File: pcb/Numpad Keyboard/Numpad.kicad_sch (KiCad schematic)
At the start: 57 parts

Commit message: Updated library
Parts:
- U?: symbol Interface_Expansion:MCP23S17_SO -> vakeyboard:MCP23S17_SO; Description / Value (none) -> 10MHz 16 POR SPI SOIC-28_300mil I/O Expanders ROHS; LCSC (none) -> C47023; Manufacturer (none) -> Microchip Tech; Mfg Part # (none) -> MCP23S17T-E/SO; Package/Footprint (none) -> SOIC-28_7.5x17.9x1.27P; Type (none) -> SMD
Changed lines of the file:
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@@
     (pin "2")
   )
-  (symbol (lib_id "Interface_Expansion:MCP23S17_SO") (at 151.13 73.66 0) (unit 1)
+  (symbol (lib_id "vakeyboard:MCP23S17_SO") (at 151.13 73.66 0) (unit 1)
     (in_bom yes) (on_board yes) (fields_autoplaced)
     (property "Reference" "U?" (id 0) (at 153.1494 45.72 0)
@@
       (effects (font (size 1.27 1.27)) (justify left) hide)
     )
+    (property "Description / Value" "10MHz 16 POR SPI SOIC-28_300mil  I/O Expanders ROHS" (id 4) (at 151.13 73.66 0)
+      (effects (font (size 1.27 1.27)) hide)
+    )
+    (property "LCSC" "C47023" (id 5) (at 151.13 73.66 0)
+      (effects (font (size 1.27 1.27)) hide)
+    )
+    (property "Manufacturer" "Microchip Tech" (id 6) (at 151.13 73.66 0)
+      (effects (font (size 1.27 1.27)) hide)
+    )
+    (property "Mfg Part #" "MCP23S17T-E/SO" (id 7) (at 151.13 73.66 0)
+      (effects (font (size 1.27 1.27)) hide)
+    )
+    (property "Package/Footprint" "SOIC-28_7.5x17.9x1.27P" (id 8) (at 151.13 73.66 0)
+      (effects (font (size 1.27 1.27)) hide)
+    )
+    (property "Type" "SMD" (id 9) (at 151.13 73.66 0)
+      (effects (font (size 1.27 1.27)) hide)
+    )
+    (property "Your Instructions / Notes" "" (id 10) (at 151.13 73.66 0)
+      (effects (font (size 1.27 1.27)) hide)
+    )
     (pin "1")

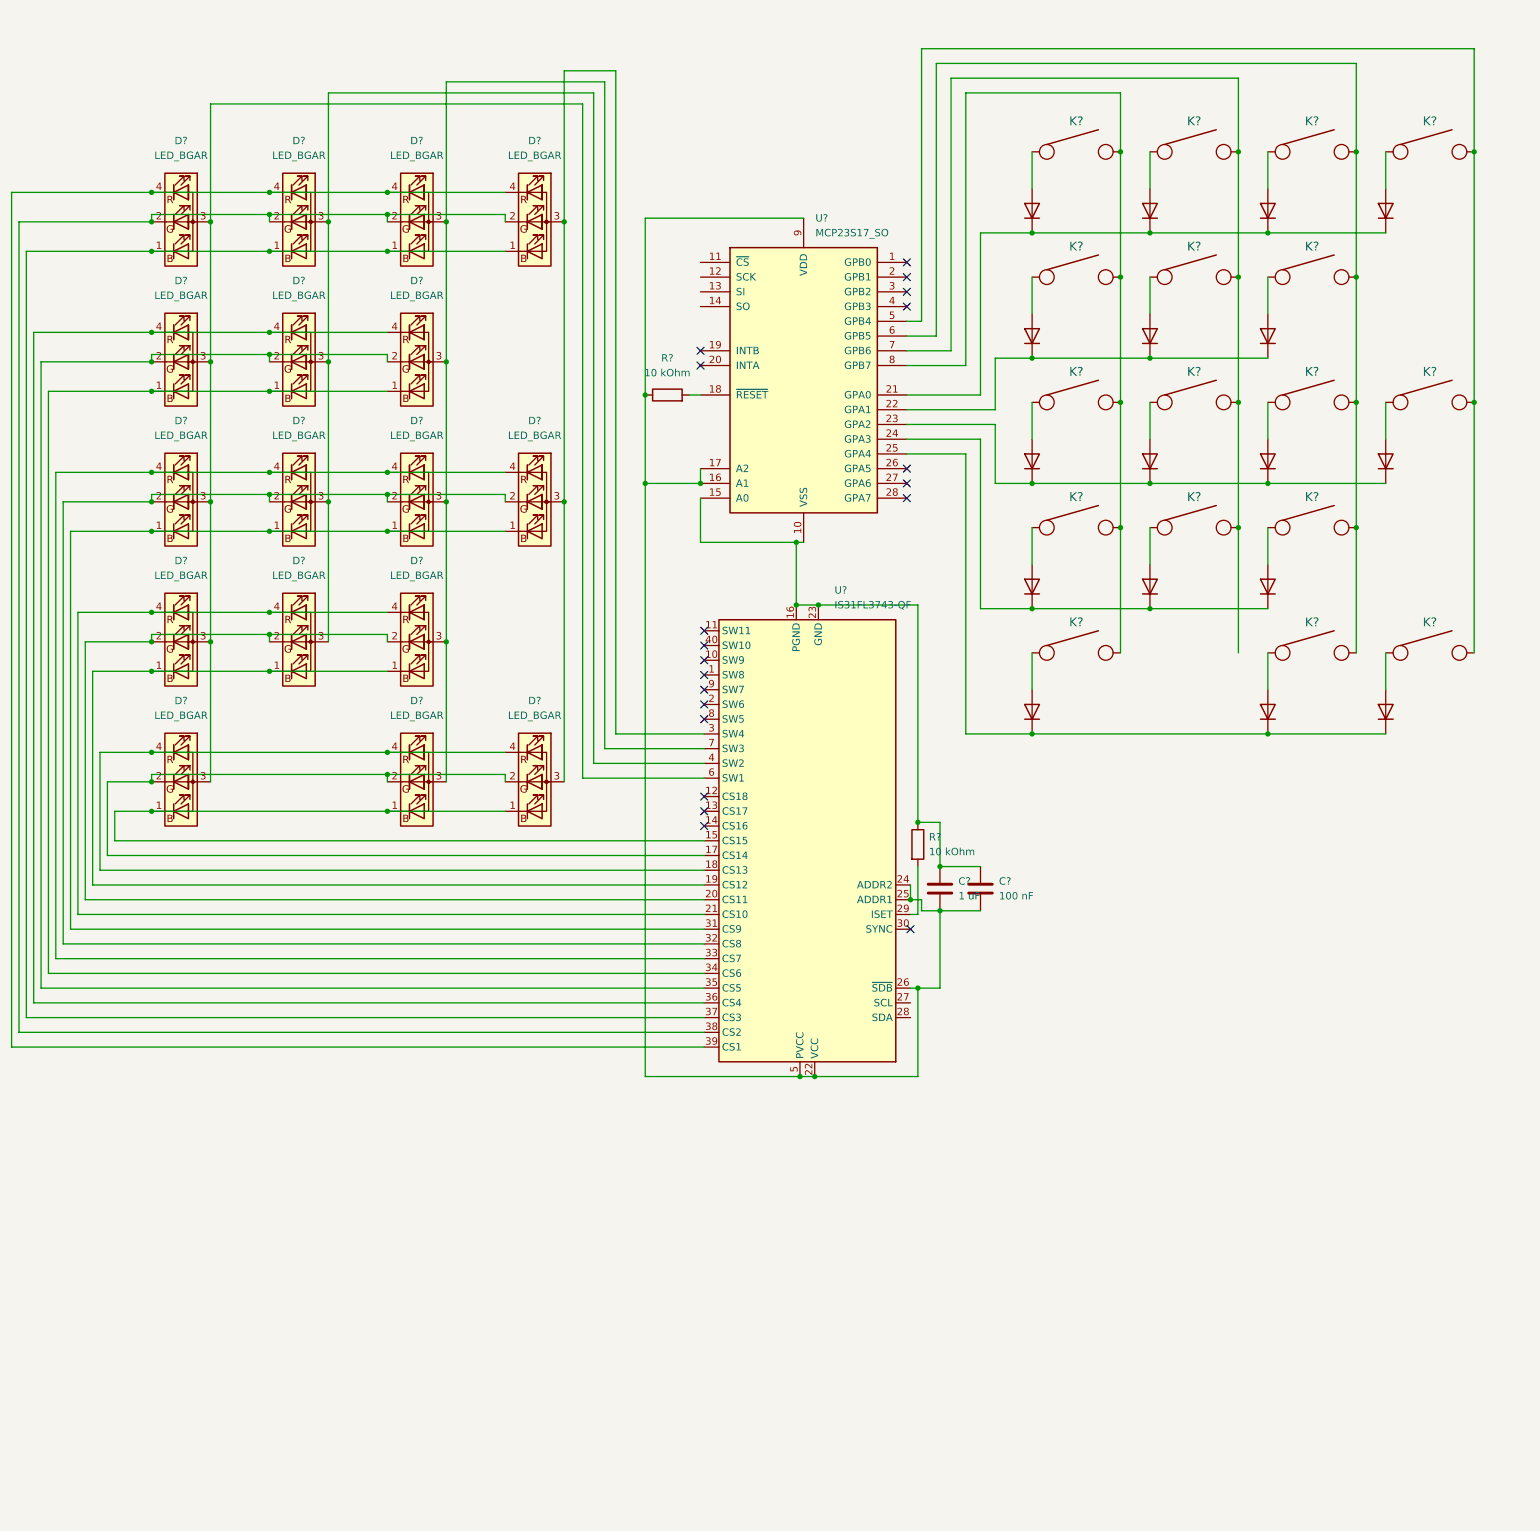
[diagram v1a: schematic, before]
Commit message: Mostly finished tracks for numpad
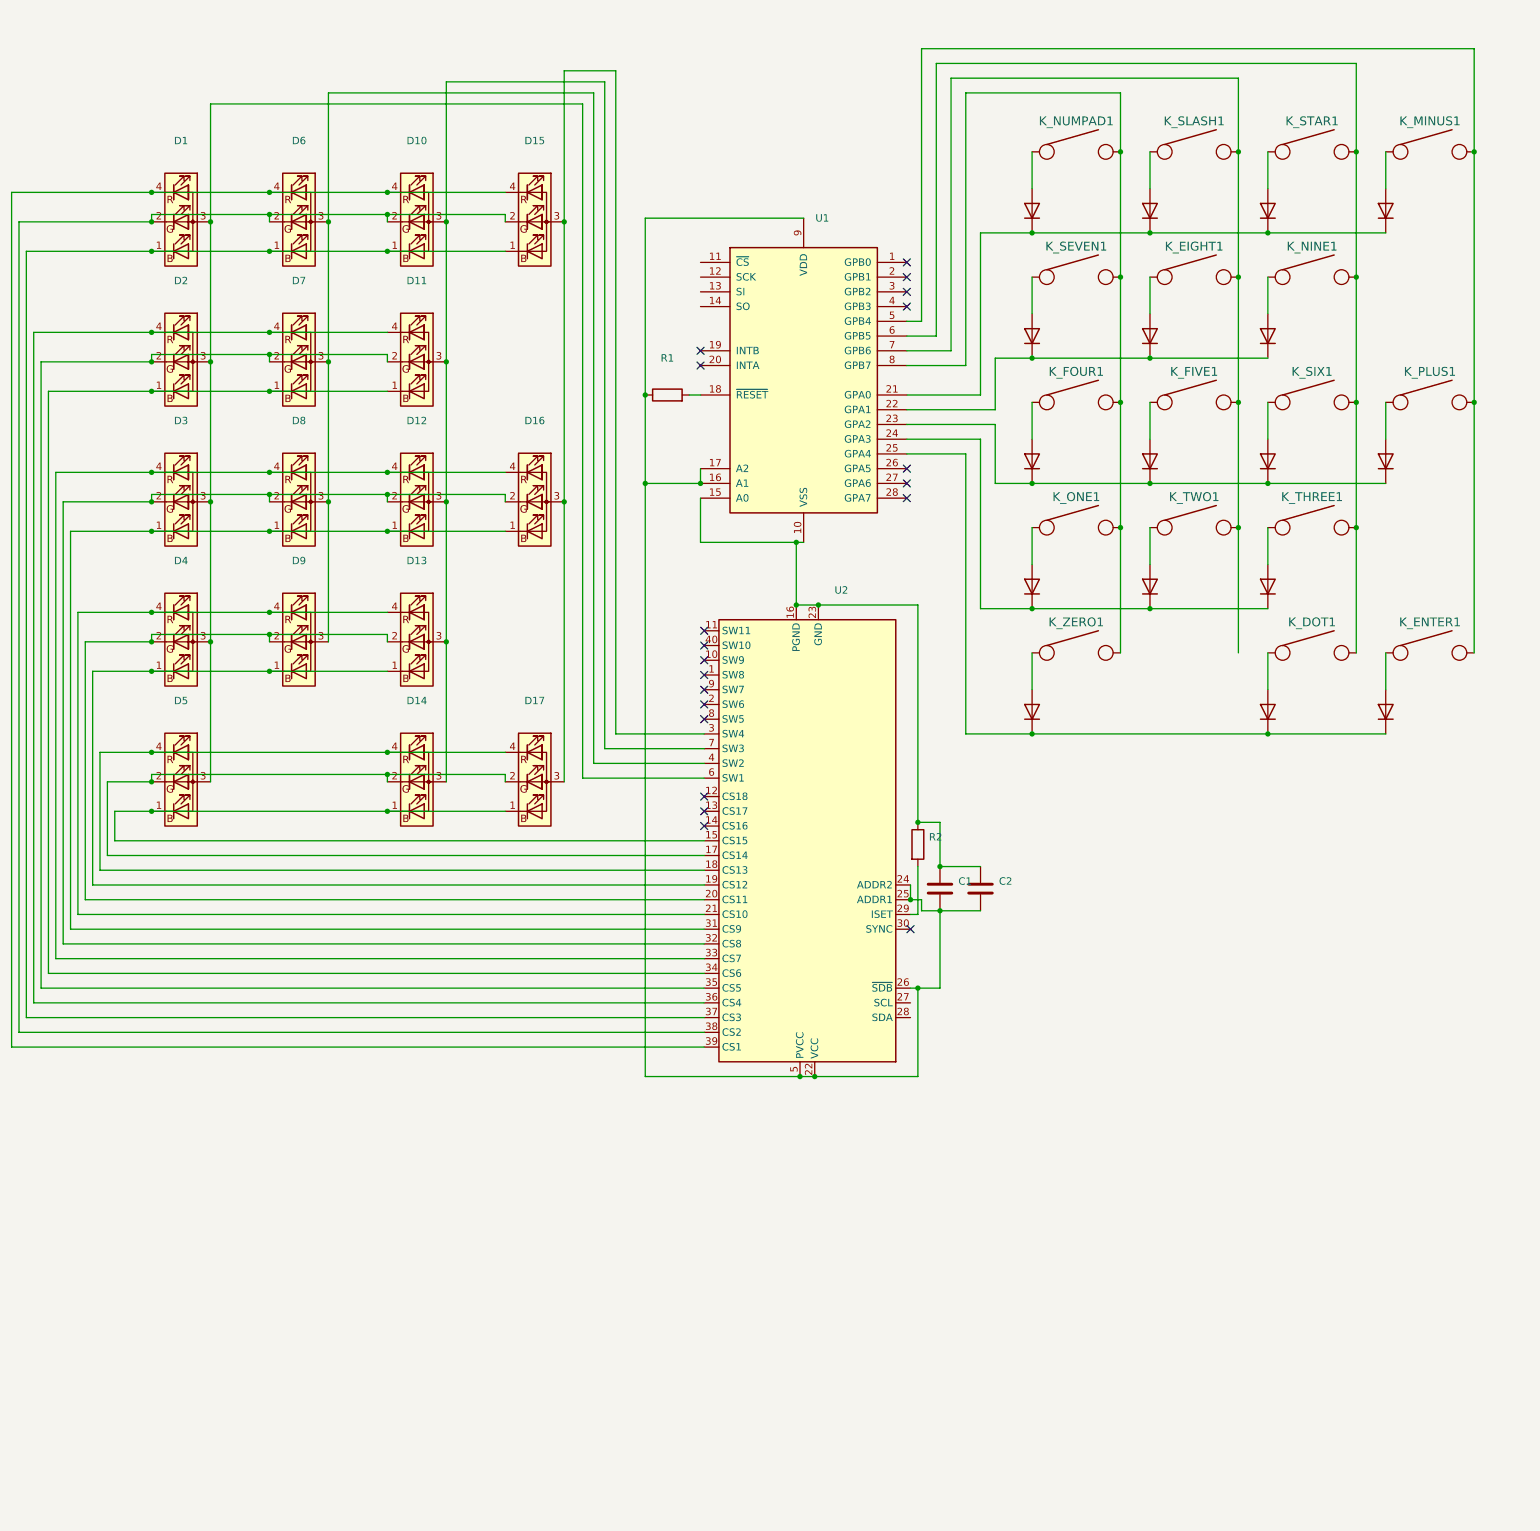
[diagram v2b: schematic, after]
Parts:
- C1: renamed from C?; value 1 uF -> C 1uF; footprint (none) -> Footprints:C_0402_1005Metric; symbol Device:C -> vakeyboard:C 1uF; Description / Value (none) -> 25V 1uF X5R ±10% 0402 Multilayer Ceramic Capacitors MLCC - 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; LCSC (none) -> C52923; Manufacturer (none) -> Samsung Electro-Mechanics; Mfg Part # (none) -> CL05A105KA5NQNC; Package/Footprint (none) -> 0402; Type (none) -> SMD
- C2: renamed from C?; value 100 nF -> C_100nF; footprint (none) -> Footprints:C_0402_1005Metric; symbol Device:C -> vakeyboard:C_100nF; Description / Value (none) -> 16V 100nF X7R ±10% 0402 Multilayer Ceramic Capacitors MLCC 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; LCSC (none) -> C1525; Manufacturer (none) -> Samsung Electro-Mechanics; Mfg Part # (none) -> CL05B104KO5NNNC; Package/Footprint (none) -> 0402; Type (none) -> SMD
- D1: renamed from D?; value LED_BGAR -> LED_NUMPAD; footprint (none) -> Footprints:19-237; symbol Device:LED_BGAR -> vakeyboard:LED; Description / Value (none) -> 5mA Colorless transparence -40℃~+85℃ Common anode RGB 120° 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; LCSC (none) -> C883183; Manufacturer (none) -> Everlight Elec; Mfg Part # (none) -> 19-237/R6GHBHC-A04/2T; Package/Footprint (none) -> 19-237; Type (none) -> SMD
- D10: renamed from D?; value LED_BGAR -> LED_STAR; footprint (none) -> Footprints:19-237; symbol Device:LED_BGAR -> vakeyboard:LED; Description / Value (none) -> 5mA Colorless transparence -40℃~+85℃ Common anode RGB 120° 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; LCSC (none) -> C883183; Manufacturer (none) -> Everlight Elec; Mfg Part # (none) -> 19-237/R6GHBHC-A04/2T; Package/Footprint (none) -> 19-237; Type (none) -> SMD
- D11: renamed from D?; value LED_BGAR -> LED9; footprint (none) -> Footprints:19-237; symbol Device:LED_BGAR -> vakeyboard:LED; Description / Value (none) -> 5mA Colorless transparence -40℃~+85℃ Common anode RGB 120° 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; LCSC (none) -> C883183; Manufacturer (none) -> Everlight Elec; Mfg Part # (none) -> 19-237/R6GHBHC-A04/2T; Package/Footprint (none) -> 19-237; Type (none) -> SMD
- D12: renamed from D?; value LED_BGAR -> LED_6; footprint (none) -> Footprints:19-237; symbol Device:LED_BGAR -> vakeyboard:LED; Description / Value (none) -> 5mA Colorless transparence -40℃~+85℃ Common anode RGB 120° 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; LCSC (none) -> C883183; Manufacturer (none) -> Everlight Elec; Mfg Part # (none) -> 19-237/R6GHBHC-A04/2T; Package/Footprint (none) -> 19-237; Type (none) -> SMD
- D13: renamed from D?; value LED_BGAR -> LED_3; footprint (none) -> Footprints:19-237; symbol Device:LED_BGAR -> vakeyboard:LED; Description / Value (none) -> 5mA Colorless transparence -40℃~+85℃ Common anode RGB 120° 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; LCSC (none) -> C883183; Manufacturer (none) -> Everlight Elec; Mfg Part # (none) -> 19-237/R6GHBHC-A04/2T; Package/Footprint (none) -> 19-237; Type (none) -> SMD
- D14: renamed from D?; value LED_BGAR -> LED_DOT; footprint (none) -> Footprints:19-237; symbol Device:LED_BGAR -> vakeyboard:LED; Description / Value (none) -> 5mA Colorless transparence -40℃~+85℃ Common anode RGB 120° 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; LCSC (none) -> C883183; Manufacturer (none) -> Everlight Elec; Mfg Part # (none) -> 19-237/R6GHBHC-A04/2T; Package/Footprint (none) -> 19-237; Type (none) -> SMD
- D15: renamed from D?; value LED_BGAR -> LED_MINUS; footprint (none) -> Footprints:19-237; symbol Device:LED_BGAR -> vakeyboard:LED; Description / Value (none) -> 5mA Colorless transparence -40℃~+85℃ Common anode RGB 120° 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; LCSC (none) -> C883183; Manufacturer (none) -> Everlight Elec; Mfg Part # (none) -> 19-237/R6GHBHC-A04/2T; Package/Footprint (none) -> 19-237; Type (none) -> SMD
- D16: renamed from D?; value LED_BGAR -> LED_PLUS; footprint (none) -> Footprints:19-237; symbol Device:LED_BGAR -> vakeyboard:LED; Description / Value (none) -> 5mA Colorless transparence -40℃~+85℃ Common anode RGB 120° 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; LCSC (none) -> C883183; Manufacturer (none) -> Everlight Elec; Mfg Part # (none) -> 19-237/R6GHBHC-A04/2T; Package/Footprint (none) -> 19-237; Type (none) -> SMD
- D17: renamed from D?; value LED_BGAR -> LED_ENTER; footprint (none) -> Footprints:19-237; symbol Device:LED_BGAR -> vakeyboard:LED; Description / Value (none) -> 5mA Colorless transparence -40℃~+85℃ Common anode RGB 120° 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; LCSC (none) -> C883183; Manufacturer (none) -> Everlight Elec; Mfg Part # (none) -> 19-237/R6GHBHC-A04/2T; Package/Footprint (none) -> 19-237; Type (none) -> SMD
- D18, D19, D20, D21, D22, D23, D24, D25, D26, D27, D28, D29, D30, D31, D32, D33, D34: renamed from D?; footprint (none) -> Diode_SMD:D_SOD-523; Description / Value (none) -> 80V -55℃~+150℃@(Tj) 1.2V@100mA 4ns 100nA@80V 100mA SOD-523 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; LCSC (none) -> C414017; Manufacturer (none) -> MDD（Microdiode Electronics）; Mfg Part # (none) -> 1N4148WT; Package/Footprint (none) -> SOD-523; Type (none) -> SMD
- D2: renamed from D?; value LED_BGAR -> LED_7; footprint (none) -> Footprints:19-237; symbol Device:LED_BGAR -> vakeyboard:LED; Description / Value (none) -> 5mA Colorless transparence -40℃~+85℃ Common anode RGB 120° 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; LCSC (none) -> C883183; Manufacturer (none) -> Everlight Elec; Mfg Part # (none) -> 19-237/R6GHBHC-A04/2T; Package/Footprint (none) -> 19-237; Type (none) -> SMD
- D3: renamed from D?; value LED_BGAR -> LED_4; footprint (none) -> Footprints:19-237; symbol Device:LED_BGAR -> vakeyboard:LED; Description / Value (none) -> 5mA Colorless transparence -40℃~+85℃ Common anode RGB 120° 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; LCSC (none) -> C883183; Manufacturer (none) -> Everlight Elec; Mfg Part # (none) -> 19-237/R6GHBHC-A04/2T; Package/Footprint (none) -> 19-237; Type (none) -> SMD
- D4: renamed from D?; value LED_BGAR -> LED_1; footprint (none) -> Footprints:19-237; symbol Device:LED_BGAR -> vakeyboard:LED; Description / Value (none) -> 5mA Colorless transparence -40℃~+85℃ Common anode RGB 120° 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; LCSC (none) -> C883183; Manufacturer (none) -> Everlight Elec; Mfg Part # (none) -> 19-237/R6GHBHC-A04/2T; Package/Footprint (none) -> 19-237; Type (none) -> SMD
- D5: renamed from D?; value LED_BGAR -> LED_0; footprint (none) -> Footprints:19-237; symbol Device:LED_BGAR -> vakeyboard:LED; Description / Value (none) -> 5mA Colorless transparence -40℃~+85℃ Common anode RGB 120° 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; LCSC (none) -> C883183; Manufacturer (none) -> Everlight Elec; Mfg Part # (none) -> 19-237/R6GHBHC-A04/2T; Package/Footprint (none) -> 19-237; Type (none) -> SMD
- D6: renamed from D?; value LED_BGAR -> LED_SLASH; footprint (none) -> Footprints:19-237; symbol Device:LED_BGAR -> vakeyboard:LED; Description / Value (none) -> 5mA Colorless transparence -40℃~+85℃ Common anode RGB 120° 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; LCSC (none) -> C883183; Manufacturer (none) -> Everlight Elec; Mfg Part # (none) -> 19-237/R6GHBHC-A04/2T; Package/Footprint (none) -> 19-237; Type (none) -> SMD
- D7: renamed from D?; value LED_BGAR -> LED_8; footprint (none) -> Footprints:19-237; symbol Device:LED_BGAR -> vakeyboard:LED; Description / Value (none) -> 5mA Colorless transparence -40℃~+85℃ Common anode RGB 120° 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; LCSC (none) -> C883183; Manufacturer (none) -> Everlight Elec; Mfg Part # (none) -> 19-237/R6GHBHC-A04/2T; Package/Footprint (none) -> 19-237; Type (none) -> SMD
- D8: renamed from D?; value LED_BGAR -> LED_5; footprint (none) -> Footprints:19-237; symbol Device:LED_BGAR -> vakeyboard:LED; Description / Value (none) -> 5mA Colorless transparence -40℃~+85℃ Common anode RGB 120° 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; LCSC (none) -> C883183; Manufacturer (none) -> Everlight Elec; Mfg Part # (none) -> 19-237/R6GHBHC-A04/2T; Package/Footprint (none) -> 19-237; Type (none) -> SMD
- D9: renamed from D?; value LED_BGAR -> LED_2; footprint (none) -> Footprints:19-237; symbol Device:LED_BGAR -> vakeyboard:LED; Description / Value (none) -> 5mA Colorless transparence -40℃~+85℃ Common anode RGB 120° 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; LCSC (none) -> C883183; Manufacturer (none) -> Everlight Elec; Mfg Part # (none) -> 19-237/R6GHBHC-A04/2T; Package/Footprint (none) -> 19-237; Type (none) -> SMD
- K_DOT1: renamed from K?; value KEYSW -> .; footprint (none) -> Footprints:CherryMX_PlateMount_HotSwap_1u; Description / Value (none) -> SMD Mechanical Keyboard Shaft ROHS; LCSC (none) -> C2803348; Manufacturer (none) -> Kailh; Mfg Part # (none) -> CPG151101S11; Package/Footprint (none) -> SMD; Type (none) -> SMD
- K_EIGHT1: renamed from K?; value KEYSW -> 8; footprint (none) -> Footprints:CherryMX_PlateMount_HotSwap_1u; Description / Value (none) -> SMD Mechanical Keyboard Shaft ROHS; LCSC (none) -> C2803348; Manufacturer (none) -> Kailh; Mfg Part # (none) -> CPG151101S11; Package/Footprint (none) -> SMD; Type (none) -> SMD
- K_ENTER1: renamed from K?; value KEYSW -> ENTER; footprint (none) -> Footprints:CherryMX_PlateMount_HotSwap_2u_90deg; Description / Value (none) -> SMD Mechanical Keyboard Shaft ROHS; LCSC (none) -> C2803348; Manufacturer (none) -> Kailh; Mfg Part # (none) -> CPG151101S11; Package/Footprint (none) -> SMD; Type (none) -> SMD
- K_FIVE1: renamed from K?; value KEYSW -> 5; footprint (none) -> Footprints:CherryMX_PlateMount_HotSwap_1u; Description / Value (none) -> SMD Mechanical Keyboard Shaft ROHS; LCSC (none) -> C2803348; Manufacturer (none) -> Kailh; Mfg Part # (none) -> CPG151101S11; Package/Footprint (none) -> SMD; Type (none) -> SMD
- K_FOUR1: renamed from K?; value KEYSW -> 4; footprint (none) -> Footprints:CherryMX_PlateMount_HotSwap_1u; Description / Value (none) -> SMD Mechanical Keyboard Shaft ROHS; LCSC (none) -> C2803348; Manufacturer (none) -> Kailh; Mfg Part # (none) -> CPG151101S11; Package/Footprint (none) -> SMD; Type (none) -> SMD
- K_MINUS1: renamed from K?; value KEYSW -> -; footprint (none) -> Footprints:CherryMX_PlateMount_HotSwap_1u; Description / Value (none) -> SMD Mechanical Keyboard Shaft ROHS; LCSC (none) -> C2803348; Manufacturer (none) -> Kailh; Mfg Part # (none) -> CPG151101S11; Package/Footprint (none) -> SMD; Type (none) -> SMD
- K_NINE1: renamed from K?; value KEYSW -> 9; footprint (none) -> Footprints:CherryMX_PlateMount_HotSwap_1u; Description / Value (none) -> SMD Mechanical Keyboard Shaft ROHS; LCSC (none) -> C2803348; Manufacturer (none) -> Kailh; Mfg Part # (none) -> CPG151101S11; Package/Footprint (none) -> SMD; Type (none) -> SMD
- K_NUMPAD1: renamed from K?; value KEYSW -> NUMPAD; footprint (none) -> Footprints:CherryMX_PlateMount_HotSwap_1u; Description / Value (none) -> SMD Mechanical Keyboard Shaft ROHS; LCSC (none) -> C2803348; Manufacturer (none) -> Kailh; Mfg Part # (none) -> CPG151101S11; Package/Footprint (none) -> SMD; Type (none) -> SMD
- K_ONE1: renamed from K?; value KEYSW -> 1; footprint (none) -> Footprints:CherryMX_PlateMount_HotSwap_1u; Description / Value (none) -> SMD Mechanical Keyboard Shaft ROHS; LCSC (none) -> C2803348; Manufacturer (none) -> Kailh; Mfg Part # (none) -> CPG151101S11; Package/Footprint (none) -> SMD; Type (none) -> SMD
- K_PLUS1: renamed from K?; value KEYSW -> +; footprint (none) -> Footprints:CherryMX_PlateMount_HotSwap_2u_90deg; Description / Value (none) -> SMD Mechanical Keyboard Shaft ROHS; LCSC (none) -> C2803348; Manufacturer (none) -> Kailh; Mfg Part # (none) -> CPG151101S11; Package/Footprint (none) -> SMD; Type (none) -> SMD
- K_SEVEN1: renamed from K?; value KEYSW -> 7; footprint (none) -> Footprints:CherryMX_PlateMount_HotSwap_1u; Description / Value (none) -> SMD Mechanical Keyboard Shaft ROHS; LCSC (none) -> C2803348; Manufacturer (none) -> Kailh; Mfg Part # (none) -> CPG151101S11; Package/Footprint (none) -> SMD; Type (none) -> SMD
- K_SIX1: renamed from K?; value KEYSW -> 6; footprint (none) -> Footprints:CherryMX_PlateMount_HotSwap_1u; Description / Value (none) -> SMD Mechanical Keyboard Shaft ROHS; LCSC (none) -> C2803348; Manufacturer (none) -> Kailh; Mfg Part # (none) -> CPG151101S11; Package/Footprint (none) -> SMD; Type (none) -> SMD
- K_SLASH1: renamed from K?; value KEYSW -> /; footprint (none) -> Footprints:CherryMX_PlateMount_HotSwap_1u; Description / Value (none) -> SMD Mechanical Keyboard Shaft ROHS; LCSC (none) -> C2803348; Manufacturer (none) -> Kailh; Mfg Part # (none) -> CPG151101S11; Package/Footprint (none) -> SMD; Type (none) -> SMD
- K_STAR1: renamed from K?; value KEYSW -> *; footprint (none) -> Footprints:CherryMX_PlateMount_HotSwap_1u; Description / Value (none) -> SMD Mechanical Keyboard Shaft ROHS; LCSC (none) -> C2803348; Manufacturer (none) -> Kailh; Mfg Part # (none) -> CPG151101S11; Package/Footprint (none) -> SMD; Type (none) -> SMD
- K_THREE1: renamed from K?; value KEYSW -> 3; footprint (none) -> Footprints:CherryMX_PlateMount_HotSwap_1u; Description / Value (none) -> SMD Mechanical Keyboard Shaft ROHS; LCSC (none) -> C2803348; Manufacturer (none) -> Kailh; Mfg Part # (none) -> CPG151101S11; Package/Footprint (none) -> SMD; Type (none) -> SMD
- K_TWO1: renamed from K?; value KEYSW -> 2; footprint (none) -> Footprints:CherryMX_PlateMount_HotSwap_1u; Description / Value (none) -> SMD Mechanical Keyboard Shaft ROHS; LCSC (none) -> C2803348; Manufacturer (none) -> Kailh; Mfg Part # (none) -> CPG151101S11; Package/Footprint (none) -> SMD; Type (none) -> SMD
- K_ZERO1: renamed from K?; value KEYSW -> 0; footprint (none) -> Footprints:CherryMX_PlateMount_HotSwap_2u; Description / Value (none) -> SMD Mechanical Keyboard Shaft ROHS; LCSC (none) -> C2803348; Manufacturer (none) -> Kailh; Mfg Part # (none) -> CPG151101S11; Package/Footprint (none) -> SMD; Type (none) -> SMD
- R1, R2: renamed from R?; value 10 kOhm -> R; footprint (none) -> Footprints:R_0402_1005Metric; symbol Device:R -> vakeyboard:R; Description / Value (none) -> 1/16W Thick Film Resistors 50V ±1% ±100ppm/℃ -55℃~+155℃ 10k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; LCSC (none) -> C25744; Manufacturer (none) -> UNI-ROYAL(Uniroyal Elec); Mfg Part # (none) -> 0402WGF1002TCE; Package/Footprint (none) -> 0402; Type (none) -> SMD
- U2: renamed from U?; footprint (none) -> Footprints:QFN-40-1EP_5x5mm_P0.4mm_EP3.4x3.4mm; Description / Value (none) -> 10MHz 16 POR SPI SOIC-28_300mil I/O Expanders ROHS; LCSC (none) -> C47023; Manufacturer (none) -> Microchip Tech; Mfg Part # (none) -> MCP23S17T-E/SO; Package/Footprint (none) -> SOIC-28_7.5x17.9x1.27P; Type (none) -> SMD
- gave numbers to parts that had none: 1
